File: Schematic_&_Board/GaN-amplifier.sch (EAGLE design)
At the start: 80 parts, among them IC1 LT3080, J1 JOHNSON_SMA_EDGE_LAUNCH_142-0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, J2 JOHNSON_SMA_EDGE_LAUNCH_142-0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, Q1 MMBT3906LT1SMD, T1 IPB080N03L G, T2 IPB080N03L G, T3 IPB080N03L G, T4 IPB080N03L G, T5 BSP89, U1 TPS7A30XX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

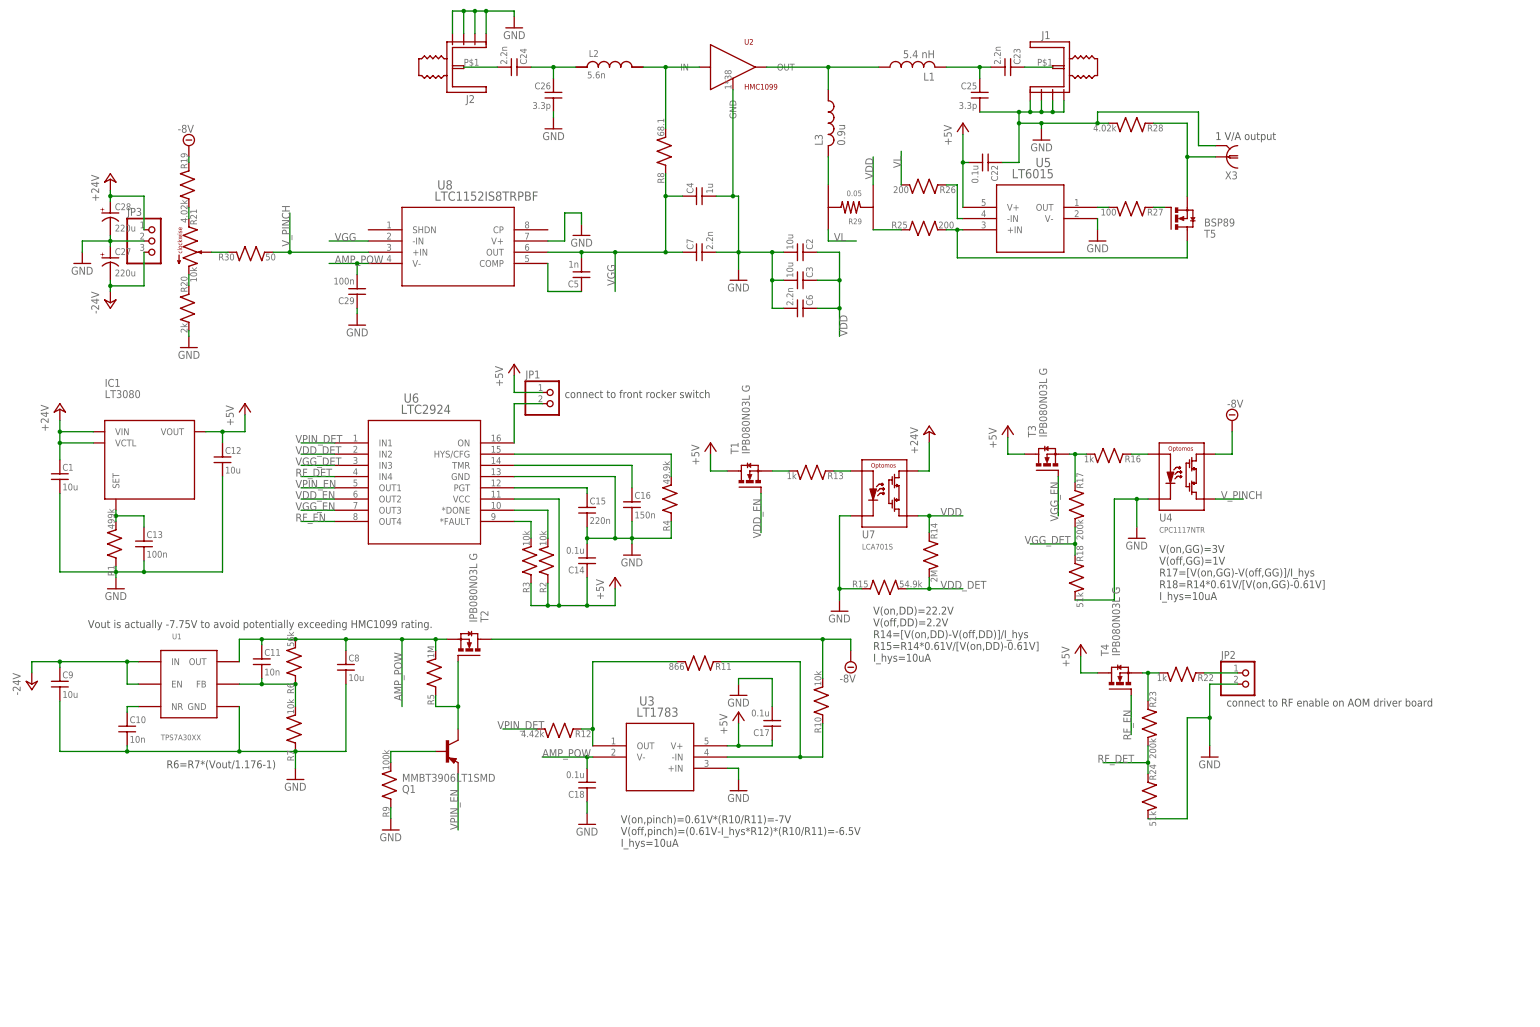
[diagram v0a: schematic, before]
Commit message: Added Error Monitor LEDs
Added a couple LEDs to indicate the status of the power sequencer.

DSB
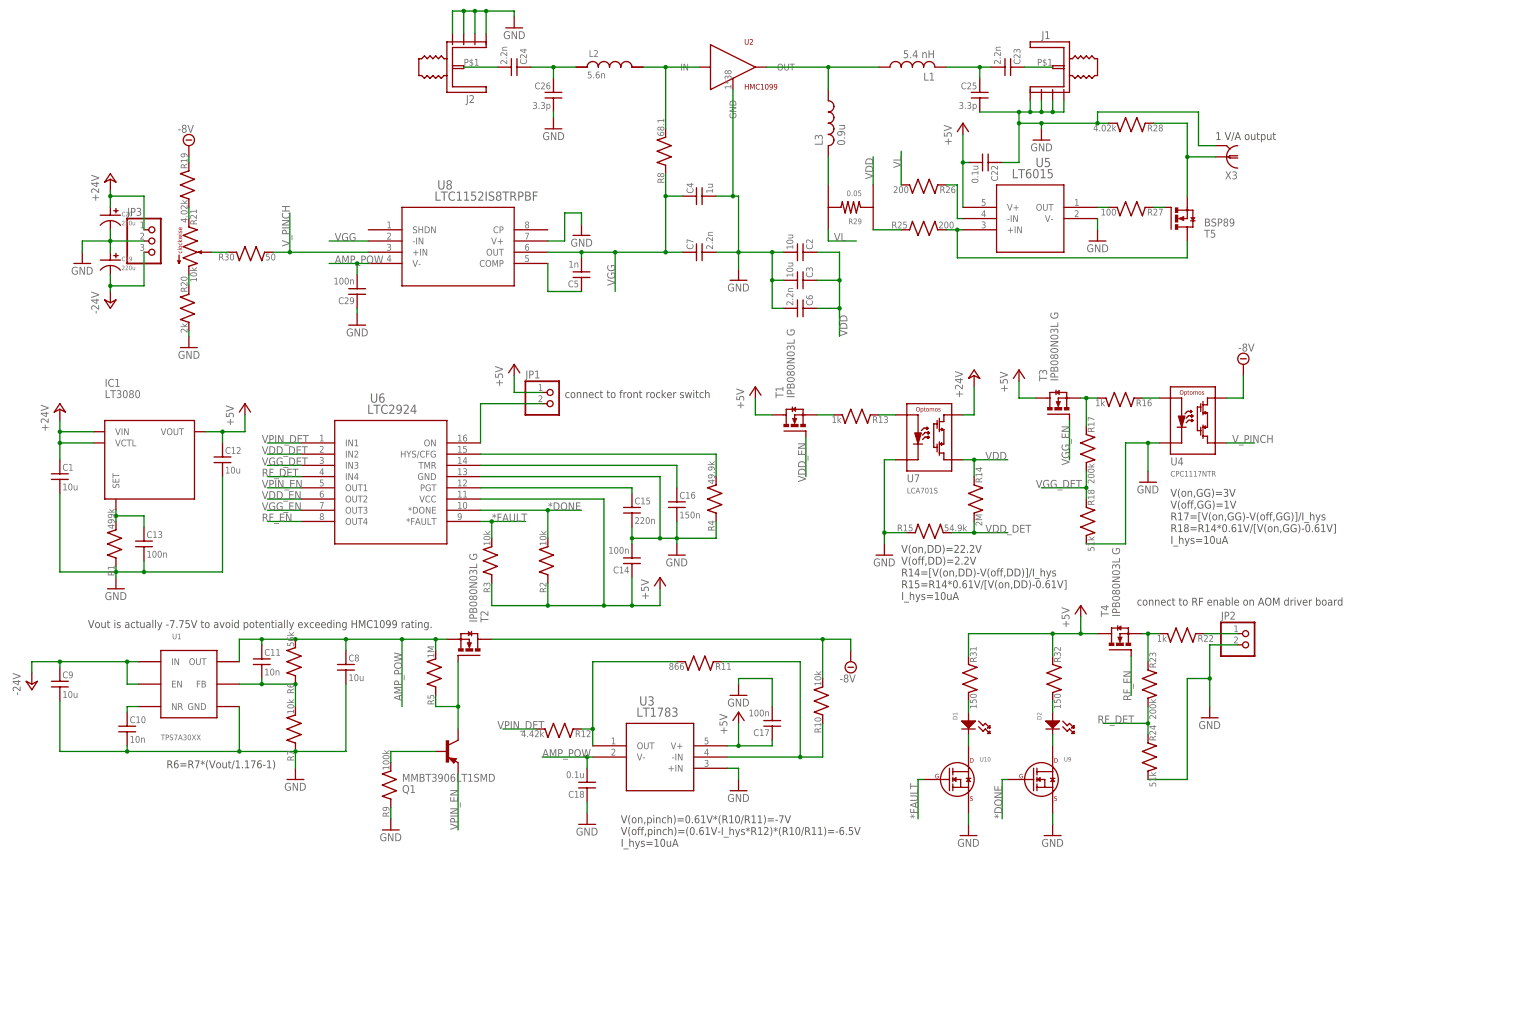
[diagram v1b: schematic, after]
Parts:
- removed C27, C28: 220u, jqi_passives:C_POL_SMDF
- added C19, C20: 220u, MF_Passives:CAPACITOR_P_10MM
- added D1: (no value), MF_LEDs:LED_SINGLE-0603-GREEN
- added D2: (no value), MF_LEDs:LED_SINGLE-0603-RED
- added R31, R32: 150, jqi_passives:R_SMDR0603
- added U10, U9: (no value), MF_Discrete_Semiconductor:N-CHANNEL_FET_BSS138_SOT-23-3
- C14, C17: value 0.1u -> 100n
- Q1: PARTNO MMBT3906LT1G -> MF-DSC-SOT233-MMBT3906
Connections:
- new net *DONE: R2.2, U6.*DONE, U9.GATE
- new net *FAULT: R3.2, U10.GATE, U6.*FAULT
- new net N$18: D1.ANODE, R31.2
- new net N$37: D2.ANODE, R32.2
- net +24V: now also C20.P$1; no longer C28.+
- net +5V: now also R31.1, R32.1
- net -24V: now also C19.P$2; no longer C27.-
- net GND: now also C19.P$1, C20.P$2, U10.SOURCE, U9.SOURCE; no longer C27.+, C28.-
- net N$2: now also D1.CATHODE, U10.DRAIN; no longer R2.2, U6.*DONE
- net N$3: now also D2.CATHODE, U9.DRAIN; no longer R3.2, U6.*FAULT
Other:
- moved on the sheet: C14, C15, C16, JP2, R13, R14, R15, R16, R17, R18, R22, R23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

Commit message: QR and more LEDs
I added a few more indicator LEDs and a QR code that points to the
repository.

DSB
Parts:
- added D3, D4, D5, D6: (no value), MF_LEDs:LED_SINGLE-0603-GREEN
- added QR1: QR-HTTPS://GIT.IO/VMVF3-LIGHT-SILK, QR-git.io-vMvf3:QR-HTTPS://GIT.IO/VMVF3-LIGHT-SILK
- added R33, R34, R35: 150, jqi_passives:R_SMDR0603
- added R36: 300, jqi_passives:R_SMDR0603
- R21: value 10k -> (none)
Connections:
- new net N$38: D4.ANODE, R34.2
- new net N$39: D3.ANODE, R33.2
- new net N$40: D5.ANODE, R35.2
- new net N$41: D6.ANODE, R36.2
- net -8V: now also D6.CATHODE
- net GND: now also D3.CATHODE, D4.CATHODE, D5.CATHODE, R36.1
- net N$11: now also R34.1
- net N$14: now also R35.1
- net N$21: now also R33.1
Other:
- moved on the sheet: JP2, R16, R22, U4

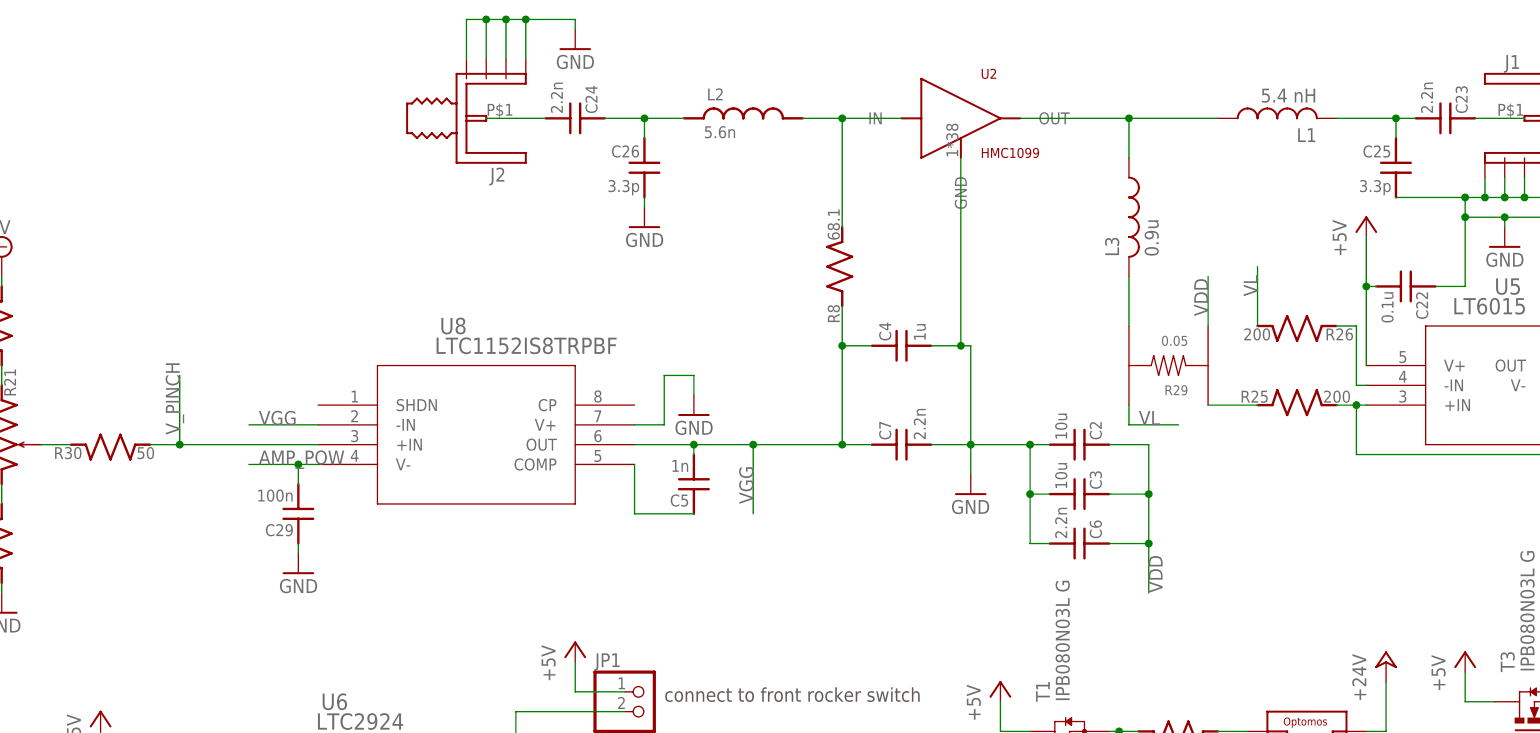
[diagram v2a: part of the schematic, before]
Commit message: Prepared to order
Made a few adjustments based on Alessandro's suggestions. Ready to order
once consigned parts arrive.

DSB
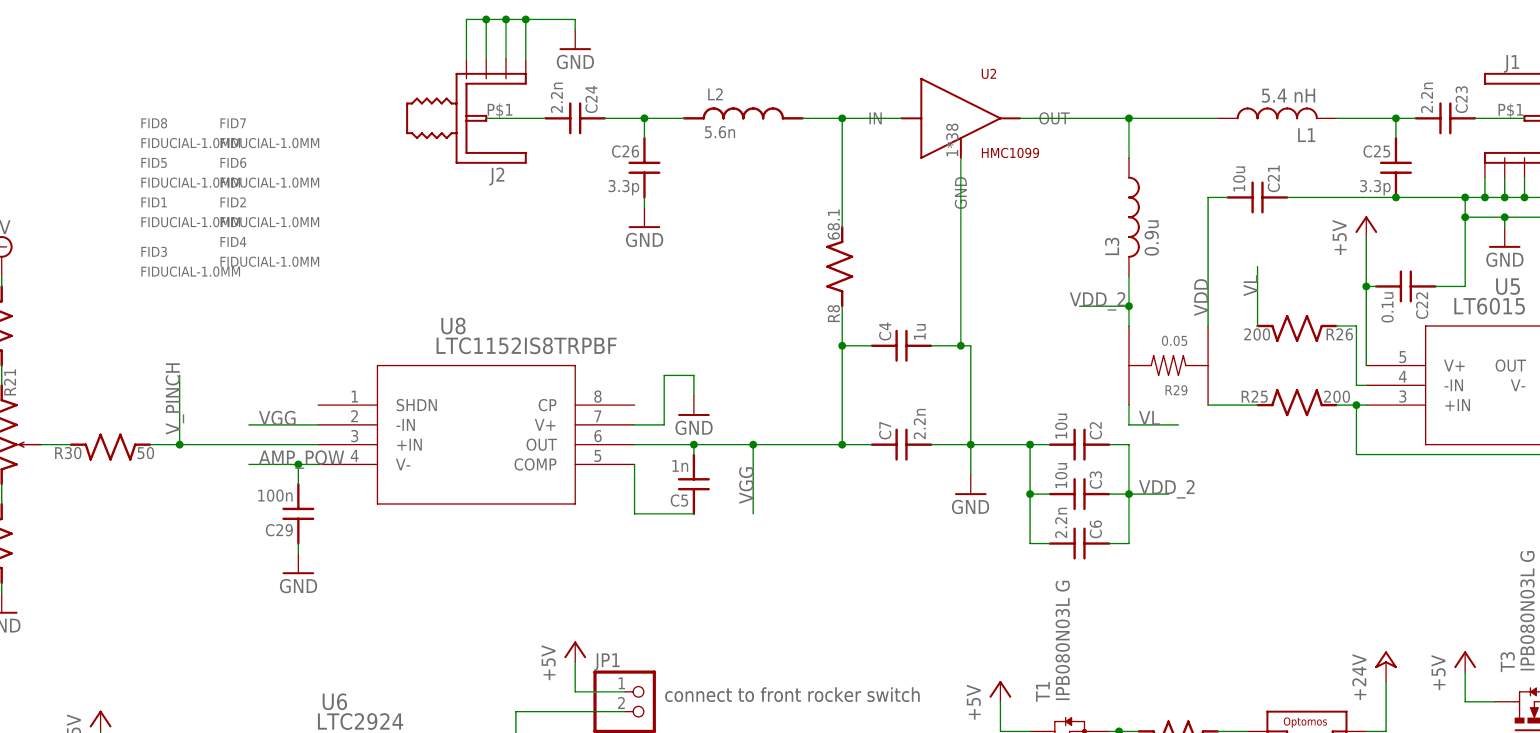
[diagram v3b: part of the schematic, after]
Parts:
- added C21: 10u, jqi_passives:C_MLCC_SMDCMLCC_1210
- added FID1, FID2, FID3, FID4, FID5, FID6, FID7, FID8: FIDUCIAL-1.0MM, fiducials-jqi:FIDUCIAL-1.0MM
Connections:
- removed net N$23: L3.2, R29.I$2
- new net VDD_2: C2.1, C3.1, C6.1, L3.2, R29.I$2
- net GND: now also C21.1
- net VDD: now also C21.2; no longer C2.1, C3.1, C6.1
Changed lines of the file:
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@@
 </part>
 <part name="QR1" library="QR-git.io-vMvf3" deviceset="QR-HTTPS://GIT.IO/VMVF3" device="-LIGHT-SILK"/>
+<part name="FID1" library="fiducials-jqi" deviceset="FIDUCIAL" device="-1.0MM"/>
+<part name="FID2" library="fiducials-jqi" deviceset="FIDUCIAL" device="-1.0MM"/>
+<part name="FID3" library="fiducials-jqi" deviceset="FIDUCIAL" device="-1.0MM"/>
+<part name="FID4" library="fiducials-jqi" deviceset="FIDUCIAL" device="-1.0MM"/>
+<part name="C21" library="jqi_passives" deviceset="C_MLCC_SMD" device="CMLCC_1210" value="10u">
+<attribute name="PARTNO" value="UMK325C7106MM-T"/>
+</part>
+<part name="FID5" library="fiducials-jqi" deviceset="FIDUCIAL" device="-1.0MM"/>
+<part name="FID6" library="fiducials-jqi" deviceset="FIDUCIAL" device="-1.0MM"/>
+<part name="FID7" library="fiducials-jqi" deviceset="FIDUCIAL" device="-1.0MM"/>
+<part name="FID8" library="fiducials-jqi" deviceset="FIDUCIAL" device="-1.0MM"/>
 </parts>
 <sheets>
@@
 </instance>
 <instance part="QR1" gate="G$1" x="194.31" y="162.56"/>
+<instance part="FID1" gate="G$1" x="-6.35" y="209.55"/>
+<instance part="FID2" gate="G$1" x="3.81" y="209.55"/>
+<instance part="FID3" gate="G$1" x="-6.35" y="203.2"/>
+<instance part="FID4" gate="G$1" x="3.81" y="204.47"/>
+<instance part="C21" gate="G$1" x="138.43" y="210.82" rot="MR90">
+<attribute name="PARTNO" x="138.43" y="210.82" size="1.778" layer="96" display="off"/>
+</instance>
+<instance part="FID5" gate="G$1" x="-6.35" y="214.63"/>
+<instance part="FID6" gate="G$1" x="3.81" y="214.63"/>
+<instance part="FID7" gate="G$1" x="3.81" y="219.71"/>
+<instance part="FID8" gate="G$1" x="-6.35" y="219.71"/>
 </instances>
 <busses>
@@
 <wire x1="173.99" y1="210.82" x2="171.45" y2="210.82" width="0.1524" layer="91"/>
 <junction x="171.45" y="210.82"/>
+<pinref part="C21" gate="G$1" pin="1"/>
+<wire x1="140.97" y1="210.82" x2="154.94" y2="210.82" width="0.1524" layer="91"/>
+<junction x="154.94" y="210.82"/>
 </segment>
 <segment>
@@
 </segment>
 <segment>
-<pinref part="C2" gate="G$1" pin="1"/>
-<wire x1="123.19" y1="179.07" x2="118.11" y2="179.07" width="0.1524" layer="91"/>
-<pinref part="C3" gate="G$1" pin="1"/>
-<wire x1="118.11" y1="172.72" x2="123.19" y2="172.72" width="0.1524" layer="91"/>
-<wire x1="123.19" y1="172.72" x2="123.19" y2="179.07" width="0.1524" layer="91"/>
-<pinref part="C6" gate="G$1" pin="1"/>
-<wire x1="118.11" y1="166.37" x2="123.19" y2="166.37" width="0.1524" layer="91"/>
-<wire x1="123.19" y1="166.37" x2="123.19" y2="172.72" width="0.1524" layer="91"/>
-<junction x="123.19" y="172.72"/>
-<label x="123.19" y="160.02" size="1.778" layer="95" rot="MR90"/>
-<wire x1="123.19" y1="166.37" x2="123.19" y2="160.02" width="0.1524" layer="91"/>
-<junction x="123.19" y="166.37"/>
-</segment>
-<segment>
 <pinref part="R29" gate="G$1" pin="I$1"/>
-<wire x1="130.81" y1="194.31" x2="130.81" y2="200.66" width="0.1524" layer="91"/>
 <label x="130.81" y="195.58" size="1.778" layer="95" rot="R90"/>
+<pinref part="C21" gate="G$1" pin="2"/>
+<wire x1="130.81" y1="194.31" x2="130.81" y2="210.82" width="0.1524" layer="91"/>
+<wire x1="130.81" y1="210.82" x2="133.35" y2="210.82" width="0.1524" layer="91"/>
 </segment>
 </net>
@@
 </segment>
 </net>
-<net name="N$23" class="0">
+<net name="VDD_2" class="0">
 <segment>
 <pinref part="R29" gate="G$1" pin="I$2"/>
 <pinref part="L3" gate="G$1" pin="2"/>
-<wire x1="120.65" y1="194.31" x2="120.65" y2="200.66" width="0.1524" layer="91"/>
-</segment>
-</net>
+<wire x1="120.65" y1="194.31" x2="120.65" y2="196.85" width="0.1524" layer="91"/>
+<wire x1="120.65" y1="196.85" x2="120.65" y2="200.66" width="0.1524" layer="91"/>
+<wire x1="120.65" y1="196.85" x2="114.3" y2="196.85" width="0.1524" layer="91"/>
+<junction x="120.65" y="196.85"/>
+<label x="113.03" y="196.85" size="1.778" layer="95"/>
+</segment>
+<segment>
+<pinref part="C2" gate="G$1" pin="1"/>
+<wire x1="118.11" y1="179.07" x2="120.65" y2="179.07" width="0.1524" layer="91"/>
+<wire x1="120.65" y1="179.07" x2="120.65" y2="172.72" width="0.1524" layer="91"/>
+<pinref part="C3" gate="G$1" pin="1"/>
+<wire x1="120.65" y1="172.72" x2="118.11" y2="172.72" width="0.1524" layer="91"/>
+<pinref part="C6" gate="G$1" pin="1"/>
+<wire x1="120.65" y1="172.72" x2="120.65" y2="166.37" width="0.1524" layer="91"/>
+<wire x1="120.65" y1="166.37" x2="118.11" y2="166.37" width="0.1524" layer="91"/>
+<junction x="120.65" y="172.72"/>
+<wire x1="120.65" y1="172.72" x2="125.73" y2="172.72" width="0.1524" layer="91"/>
+<label x="121.92" y="172.72" size="1.778" layer="95"/>
+</segment>
+</net>
